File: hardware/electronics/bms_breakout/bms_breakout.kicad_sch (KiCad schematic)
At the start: 64 parts, among them J1 Conn_01x03_Socket, Q2 VAL, Q3 VAL, U1 BQ76905, U2 BQ25798RQMR

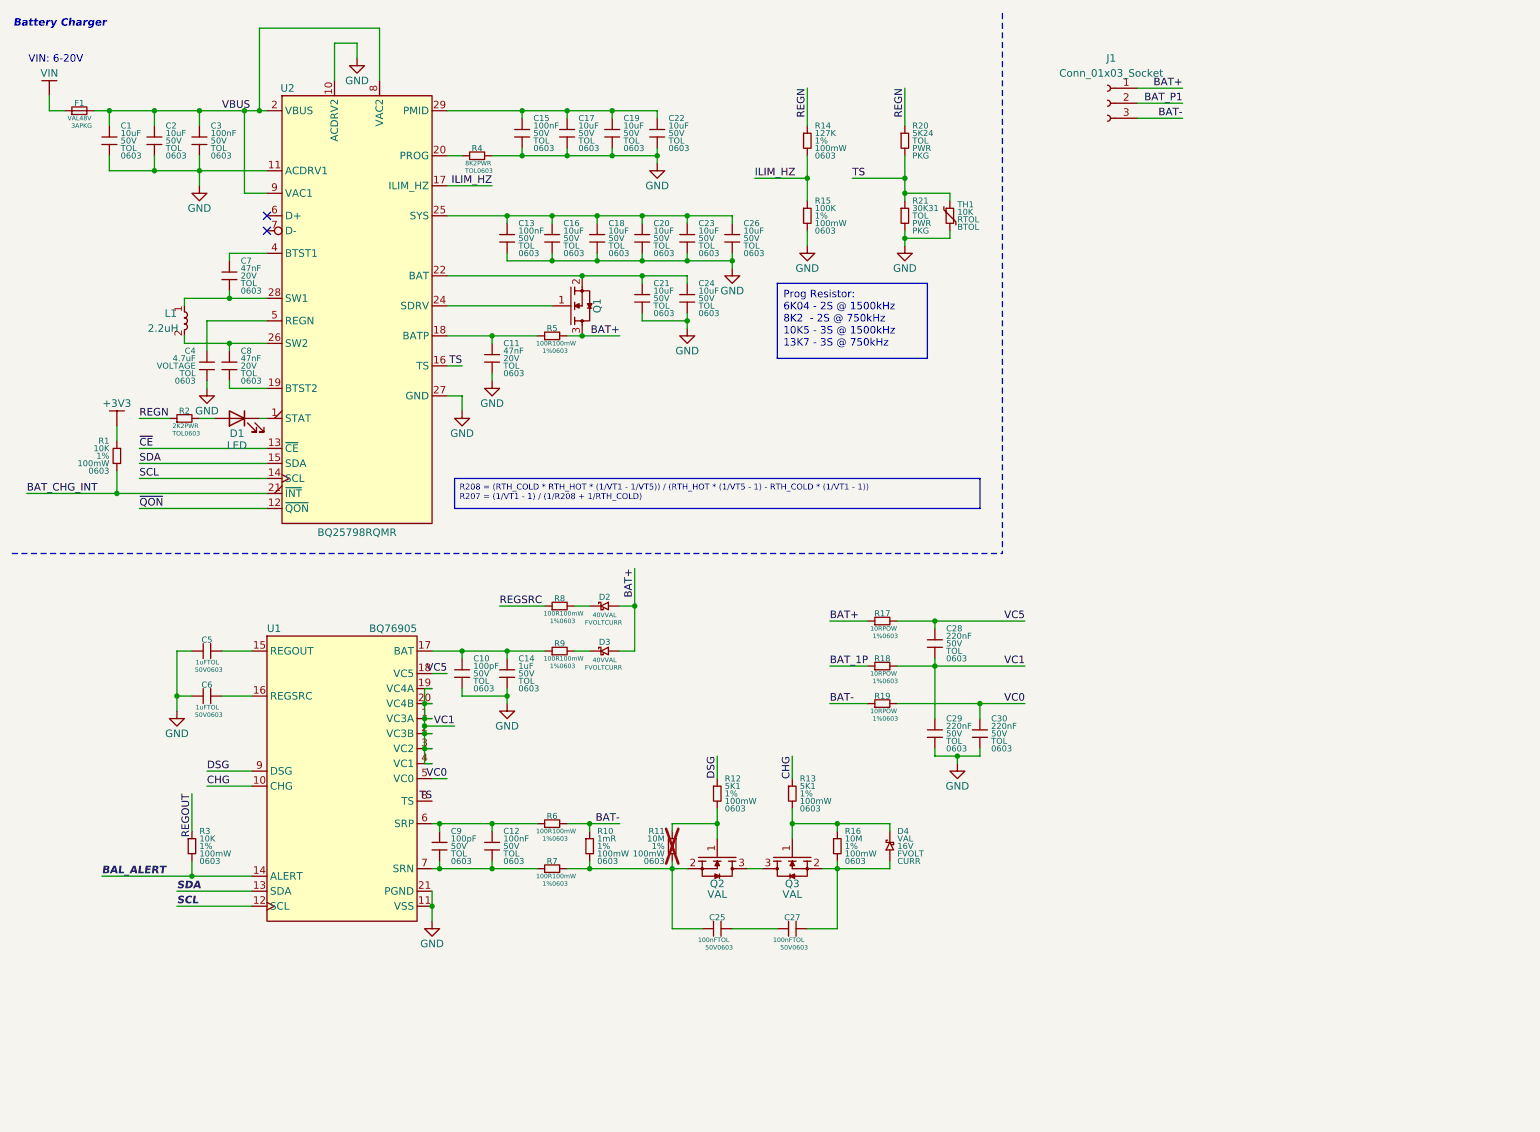
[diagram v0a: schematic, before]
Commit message: Relocated library files
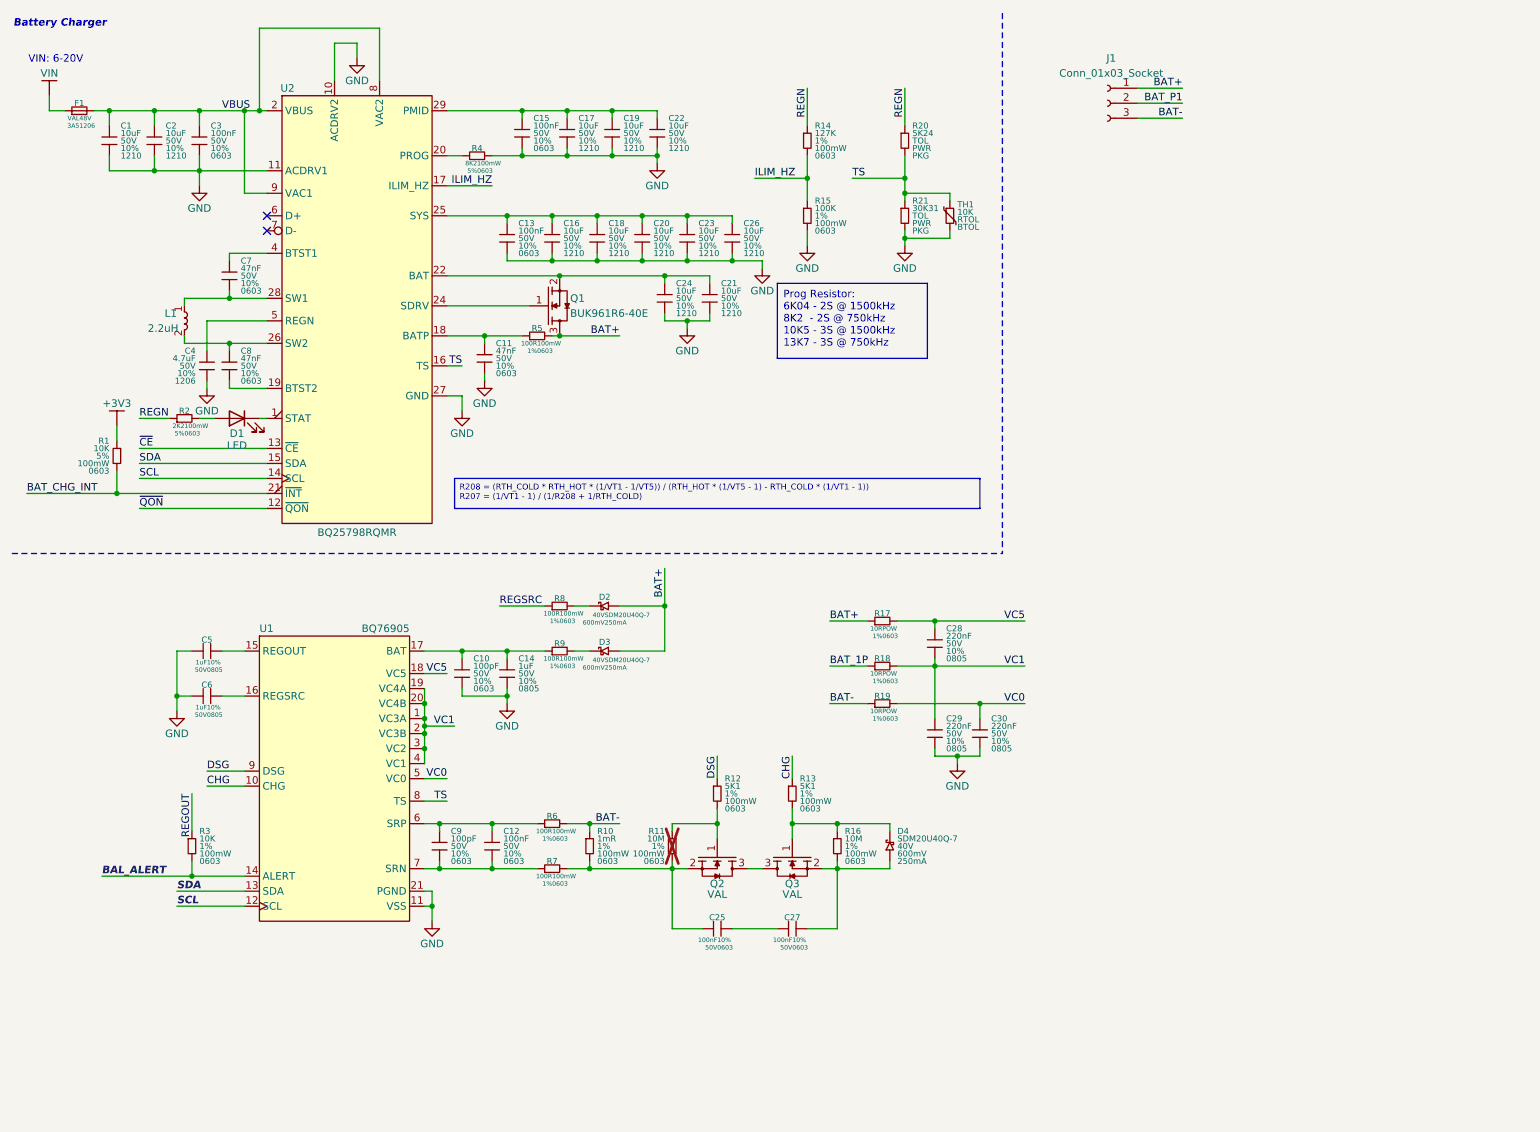
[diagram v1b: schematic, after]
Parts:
- C1, C16, C17, C18, C19, C2, C20, C21, C22, C23, C24, C26: DKPN (none) -> 478-KAM32LR71H106KUCT-ND; MPN (none) -> 12105C106K4T2A; Manufacturer (none) -> KYOCERA AVX; Package 0603 -> 1210; Tolerance TOL -> 10%
- C10, C9: footprint (none) -> DSE-Capacitors-SMD:CAPC160X80X88L35N; DKPN (none) -> 478-06035C101K4T2ACT-ND; MPN (none) -> 06035C101K4T2A; Manufacturer (none) -> KYOCERA AVX; Tolerance TOL -> 10%
- C11, C7, C8: footprint (none) -> DSE-Capacitors-SMD:CAPC160X80X88L35N; DKPN (none) -> 478-KAM15AR71H473KMCT-ND; MPN (none) -> 06035C473K4T4A; Manufacturer (none) -> KYOCERA AVX; Tolerance TOL -> 10%; Voltage Rating 20V -> 50V
- C12, C13, C15, C3: footprint (none) -> DSE-Capacitors-SMD:CAPC160X80X88L35N; DKPN (none) -> 478-KAM15AR71H104KMCT-ND; MPN (none) -> 06035C104K4T4A; Manufacturer (none) -> KYOCERA AVX; Tolerance TOL -> 10%
- C14: footprint (none) -> DSE-Capacitors-SMD:CAPC200X125X88L50N; DKPN (none) -> 478-KAM21KR71H105KUCT-ND; MPN (none) -> 08055C105K4T2A; Manufacturer (none) -> KYOCERA AVX; Package 0603 -> 0805; Tolerance TOL -> 10%; populate 1 -> (none)
- C25, C27: footprint (none) -> DSE-Capacitors-SMD:CAPC160X80X88L35N; DKPN (none) -> 478-KAM15AR71H104KMCT-ND; MPN (none) -> 06035C104K4T4A; Manufacturer (none) -> KYOCERA AVX; Tolerace TOL -> 10%
- C28, C29, C30: footprint (none) -> DSE-Capacitors-SMD:CAPC200X125X88L50N; DKPN (none) -> 478-KAM21KR71H224KLCT-ND; MPN (none) -> 08055C224K4T4A; Manufacturer (none) -> KYOCERA AVX; Package 0603 -> 0805; Tolerance TOL -> 10%; populate 1 -> (none)
- C4: footprint (none) -> DSE-Capacitors-SMD:CAPC320X160X88L50N; DKPN (none) -> 478-KAM31GR71H475KLCT-ND; MPN (none) -> 12065C475K4T4A; Manufacturer (none) -> KYOCERA AVX; Package 0603 -> 1206; Tolerance TOL -> 10%; Voltage Rating VOLTAGE -> 50V
- C5, C6: footprint (none) -> DSE-Capacitors-SMD:CAPC200X125X88L50N; DKPN (none) -> 478-KAM21KR71H105KUCT-ND; MPN (none) -> 08055C105K4T2A; Manufacturer (none) -> KYOCERA AVX; Package 0603 -> 0805; Tolerace TOL -> 10%
- D2, D3: value VAL -> SDM20U40Q-7; Current CURR -> 250mA; DKPN (none) -> 31-SDM20U40Q-7CT-ND; Forward Voltage FVOLT -> 600mV; MPN (none) -> SDM20U40Q-7; Manufacturer (none) -> Diodes Incorporated
- D4: value VAL -> SDM20U40Q-7; Current CURR -> 250mA; DKPN (none) -> 31-SDM20U40Q-7CT-ND; Forward Voltage FVOLT -> 600mV; MPN (none) -> SDM20U40Q-7; Manufacturer (none) -> Diodes Incorporated; Reverse Voltage 16V -> 40V
- F1: DKPN (none) -> 283-PTS12066V200CT-ND; MPN (none) -> PTS12066V200; Manufacturer (none) -> Eaton - Electronics Division; Package PKG -> 1206; Trip Current 3A -> 3A5
- L1: DKPN (none) -> 283-HCM1A1105V2-2R2-RCT-ND; MPN (none) -> HCM1A1105V2-2R2-R; Manufacturer (none) -> Eaton - Electronics Division
- Q1: value ~ -> BUK961R6-40E; DKPN (none) -> 1727-1895-1-ND; ID ID -> 120A; MPN (none) -> BUK961R6-40E; Manufacturer (none) -> Nexperia USA Inc.; VDSS VDSS -> 40V; VGSTH VGSTH -> 2V1
- R1: footprint (none) -> DSE-Resistors-SMD:RESC160X80X55L30N; DKPN (none) -> 541-10KGCT-ND; MPN (none) -> CRCW060310K0JNEA; Manufacturer (none) -> Vishay Dale; Tolerance 1% -> 5%
- R10, R11, R12, R13, R14, R15, R16, R17, R18, R19, R20, R21, R3, R6, R7: footprint (none) -> DSE-Resistors-SMD:RESC160X80X55L30N
- R2: footprint (none) -> DSE-Resistors-SMD:RESC160X80X55L30N; DKPN (none) -> 541-2.2KGCT-ND; MPN (none) -> CRCW06032K20JNEA; Manufacturer (none) -> Vishay Dale; Power Rating PWR -> 100mW; Tolerance TOL -> 5%
- R4: footprint (none) -> DSE-Resistors-SMD:RESC160X80X55L30N; DKPN (none) -> 541-8.2KGCT-ND; MPN (none) -> CRCW06038K20JNEA; Manufacturer (none) -> Vishay Dale; Power Rating PWR -> 100mW; Tolerance TOL -> 5%
- R5, R8, R9: footprint (none) -> DSE-Resistors-SMD:RESC160X80X55L30N; DKPN (none) -> 541-100HCT-ND; MPN (none) -> CRCW0603100RFKEA; Manufacturer (none) -> Vishay Dale
- U2: DKPN (none) -> 296-BQ25798RQMRCT-ND
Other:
- moved on the sheet: Q1, R5, U1

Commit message: replaced power symbols
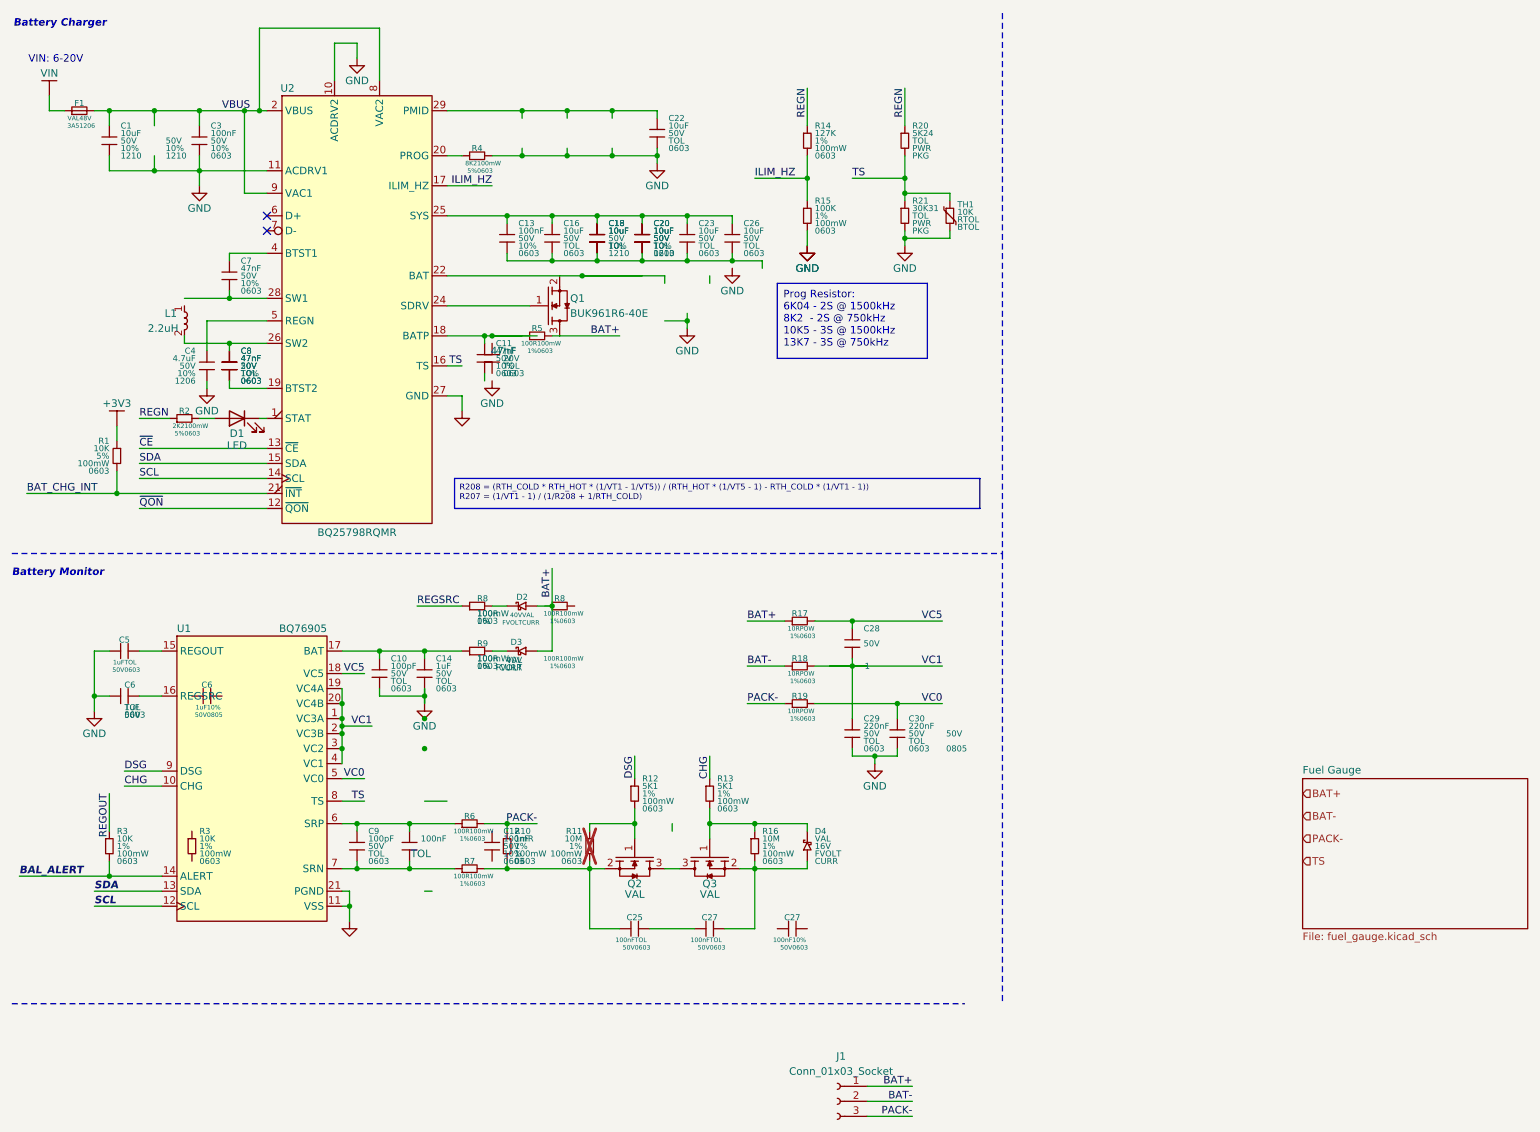
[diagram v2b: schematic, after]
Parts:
- removed C15: 100nF, DSE-Capacitors-SMD:CAPC160X80X88L35N, symbol DSE-Passives:C
- removed C17, C19, C2, C21, C24: 10uF, symbol DSE-Passives:C
- added C11, C8: 47nF, symbol DSE-Passives:C
- added C12: 100nF, symbol DSE-Passives:C
- added C18, C20: 10uF, symbol DSE-Passives:C
- added C27: 100nF, symbol DSE-Passives:C_horizontal
- added C6: 1uF, symbol DSE-Passives:C_horizontal
- added R8: 100R, symbol DSE-Passives:R_horizontal
- C10, C9: footprint DSE-Capacitors-SMD:CAPC160X80X88L35N -> (none); DKPN 478-06035C101K4T2ACT-ND -> (none); MPN 06035C101K4T2A -> (none); Manufacturer KYOCERA AVX -> (none); Tolerance 10% -> TOL
- C14: footprint DSE-Capacitors-SMD:CAPC200X125X88L50N -> (none); DKPN 478-KAM21KR71H105KUCT-ND -> (none); MPN 08055C105K4T2A -> (none); Manufacturer KYOCERA AVX -> (none); Package 0805 -> 0603; Tolerance 10% -> TOL; populate (none) -> 1
- C16, C22, C23, C26: DKPN 478-KAM32LR71H106KUCT-ND -> (none); MPN 12105C106K4T2A -> (none); Manufacturer KYOCERA AVX -> (none); Package 1210 -> 0603; Tolerance 10% -> TOL
- C25: footprint DSE-Capacitors-SMD:CAPC160X80X88L35N -> (none); MPN 06035C104K4T4A -> (none); Manufacturer KYOCERA AVX -> (none); Tolerace 10% -> TOL
- C28: value 220nF -> 100R; footprint DSE-Capacitors-SMD:CAPC200X125X88L50N -> DSE-Resistors-SMD:RESC160X80X55L30N; DKPN 478-KAM21KR71H224KLCT-ND -> 541-100HCT-ND; MPN 08055C224K4T4A -> CRCW0603100RFKEA; Manufacturer KYOCERA AVX -> Vishay Dale; Package 0805 -> 0603; Power Rating (none) -> 100mW; Tolerance 10% -> 1%; populate (none) -> 1
- C29, C30: footprint DSE-Capacitors-SMD:CAPC200X125X88L50N -> (none); DKPN 478-KAM21KR71H224KLCT-ND -> (none); MPN 08055C224K4T4A -> (none); Manufacturer KYOCERA AVX -> (none); Package 0805 -> 0603; Tolerance 10% -> TOL; populate (none) -> 1
- C5: footprint DSE-Capacitors-SMD:CAPC200X125X88L50N -> (none); MPN 08055C105K4T2A -> (none); Manufacturer KYOCERA AVX -> (none); Package 0805 -> 0603; Tolerace 10% -> TOL
- D2, D3: value SDM20U40Q-7 -> VAL; Current 250mA -> CURR; DKPN 31-SDM20U40Q-7CT-ND -> (none); Forward Voltage 600mV -> FVOLT; MPN SDM20U40Q-7 -> (none); Manufacturer Diodes Incorporated -> (none)
- D4: value SDM20U40Q-7 -> VAL; Current 250mA -> CURR; DKPN 31-SDM20U40Q-7CT-ND -> (none); Forward Voltage 600mV -> FVOLT; MPN SDM20U40Q-7 -> (none); Manufacturer Diodes Incorporated -> (none); Reverse Voltage 40V -> 16V
- R10, R11, R12, R13, R17, R18, R19, R6, R7: footprint DSE-Resistors-SMD:RESC160X80X55L30N -> (none)
- R16: footprint DSE-Resistors-SMD:RESC160X80X55L30N -> (none); populate (none) -> 1
- R9: footprint DSE-Resistors-SMD:RESC160X80X55L30N -> (none); DKPN 541-100HCT-ND -> (none); MPN CRCW0603100RFKEA -> (none); Manufacturer Vishay Dale -> (none); populate (none) -> 1
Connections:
- net BAT_1P is gone; now on net BAT-: R18.1
- net BAT_P1 is gone; now on net BAT-: J1.2 (Pin_2)
- net BAT-: no longer J1.3 (Pin_3), R10.1, R19.1, R6.2
- net GND: now also C6.1; no longer C11.2, C13.2, C16.2, C18.2, C20.2, C23.2, C26.2, C6.1
- net REGSRC: now also R8.1; no longer R8.1
- net at C9.1, R6.1, U1.6 (SRP): now also C12.1; no longer C12.1
- net at C9.2, R7.1, U1.7 (SRN): now also C12.2; no longer C12.2
- net at C13.1, C16.1, C18.1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: now also C18.1, C20.1
- net at C6.2: no longer U1.16 (REGSRC)
- net at C25.2: now also C27.1; no longer C27.1
- net at C8.2, U2.19 (BTST2): now also C8.2
- net at C8.1, L1.2, U2.26 (SW2): now also C8.1
- net at C7.2, U2.28 (SW1): no longer L1.1
- net at D4.1, Q3.2, R16.2: now also C27.2; no longer C27.2
- net at D2.2: now also R8.2; no longer R8.2
- new net: C13.2, C16.2, C18.2, C18.2, C20.2, C20.2, C23.2, C26.2
- new net: C6.2, U1.16 (REGSRC)
- new net PACK-: J1.3 (Pin_3), R10.1, R19.1, R6.2
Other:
- added sheet Fuel Gauge (fuel_gauge.kicad_sch)
- note added: "Battery Monitor"
- moved on the sheet: C10, C14, C25, C28, C5, D2, D4, J1, Q2, Q3, R10, R11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

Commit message: fixed drawing sheet ref
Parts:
- added R3: 10K, DSE-Resistors-SMD:RESC160X80X55L30N, symbol DSE-Passives:R
- C21: renamed from R3; footprint DSE-Resistors-SMD:RESC160X80X55L30N -> (none); populate (none) -> 1
- renumbered C12 to #PWR02, C9 to C15, C6 to C15, C6 to C16, R8 to C19, R9 to C22, R16 to C26, C18 to C29, C29 to C30, C30 to C9, C22 to D3, D3 to R16, C28 to R9
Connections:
- net at C11.1, U2.18 (BATP): no longer R5.1
